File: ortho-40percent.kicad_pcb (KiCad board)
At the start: 2 copper layers, 229 x 81 mm, 128 parts, among them J1 USB-C_Receptacle-24, SW1 SW_NO_4-Pin, SW10 CherryMX, SW11 CherryMX, SW12 CherryMX, SW13 CherryMX, SW14 CherryMX, SW15 CherryMX, SW16 CherryMX, SW17 CherryMX, SW18 CherryMX, SW19 CherryMX, SW2 CherryMX, SW20 CherryMX, SW21 CherryMX, SW22 CherryMX, SW23 CherryMX, SW24 CherryMX, SW25 CherryMX, SW26 CherryMX, SW27 CherryMX, SW28 CherryMX, SW29 CherryMX, SW3 CherryMX, SW30 CherryMX, SW31 CherryMX, SW32 CherryMX, SW33 CherryMX, SW34 CherryMX, SW35 CherryMX, SW36 CherryMX, SW37 CherryMX, SW38 CherryMX, SW39 CherryMX, SW4 CherryMX, SW40 CherryMX, SW41 CherryMX, SW42 CherryMX, SW43 CherryMX, SW44 CherryMX, SW45 CherryMX, SW46 CherryMX, SW47 CherryMX, SW48 CherryMX, SW49 CherryMX, SW5 CherryMX, SW50 CherryMX, SW51 CherryMX, SW6 CherryMX, SW7 CherryMX, SW8 CherryMX, SW9 CherryMX, U1 U_TPD4E05U06DQAR, U2 U_ATmega32u4-MU, Y1 XTAL_4Lead

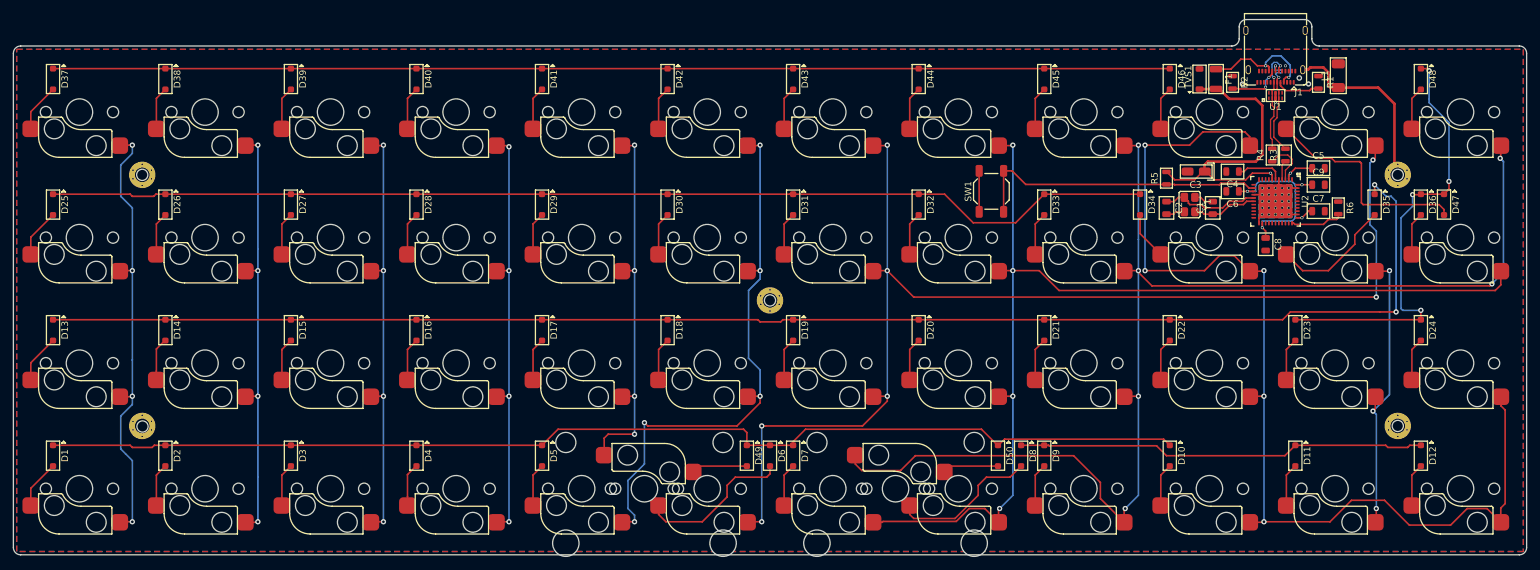
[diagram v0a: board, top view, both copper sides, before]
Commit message: Routing Finished
All connections routed. Focusing on cleaning up for length optimization and minimal bottom plane cutting.
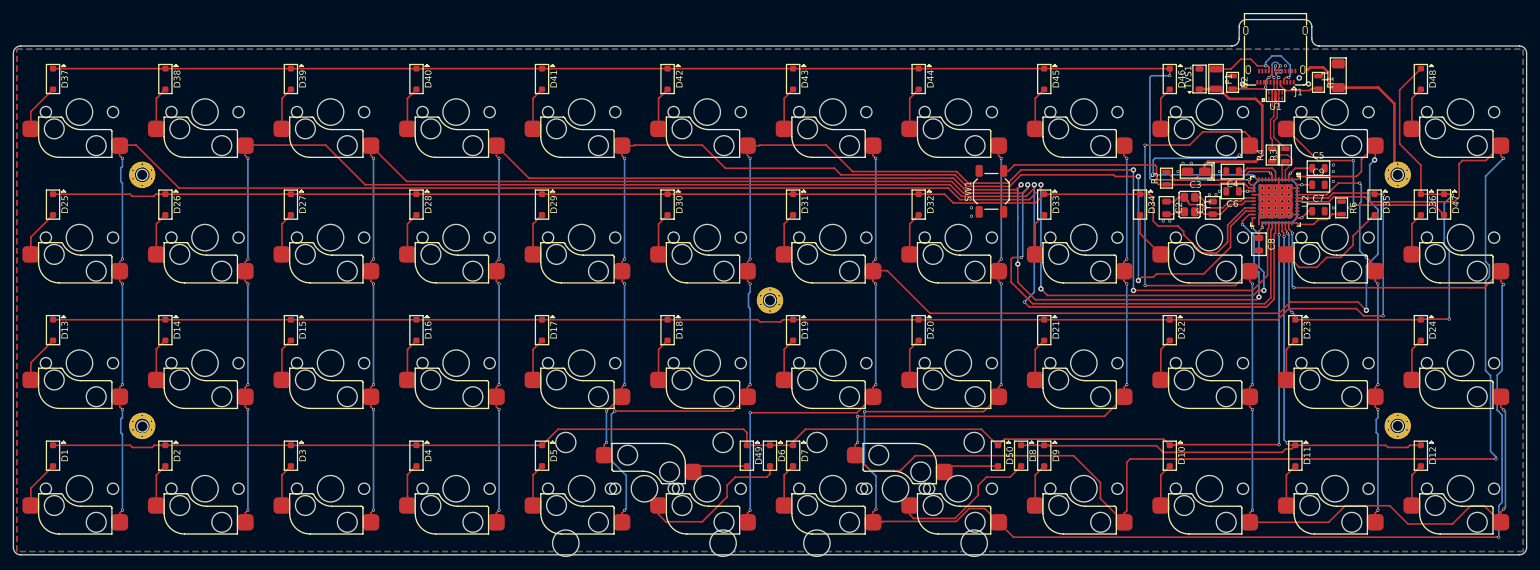
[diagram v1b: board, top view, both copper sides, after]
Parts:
- moved C8 1.00 mm to (228.5, 192.9)
- moved R6 0.50 mm to (241.0, 187.4)
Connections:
- D1 pad K: /KeyMatrix/ROW3 -> /ROW3
- D10 pad K: /KeyMatrix/ROW3 -> /ROW3
- D11 pad K: /KeyMatrix/ROW4 -> /ROW4
- D12 pad K: /KeyMatrix/ROW4 -> /ROW4
- D13 pad K: /KeyMatrix/ROW2 -> /ROW2
- D14 pad K: /KeyMatrix/ROW2 -> /ROW2
- D15 pad K: /KeyMatrix/ROW2 -> /ROW2
- D16 pad K: /KeyMatrix/ROW2 -> /ROW2
- D17 pad K: /KeyMatrix/ROW2 -> /ROW2
- D18 pad K: /KeyMatrix/ROW2 -> /ROW2
- D19 pad K: /KeyMatrix/ROW2 -> /ROW2
- D2 pad K: /KeyMatrix/ROW3 -> /ROW3
- D20 pad K: /KeyMatrix/ROW2 -> /ROW2
- D21 pad K: /KeyMatrix/ROW2 -> /ROW2
- D22 pad K: /KeyMatrix/ROW2 -> /ROW2
- D23 pad K: /KeyMatrix/ROW5 -> /ROW5
- D24 pad K: /KeyMatrix/ROW5 -> /ROW5
- D25 pad K: /KeyMatrix/ROW1 -> /ROW1
- D26 pad K: /KeyMatrix/ROW1 -> /ROW1
- D27 pad K: /KeyMatrix/ROW1 -> /ROW1
- D28 pad K: /KeyMatrix/ROW1 -> /ROW1
- D29 pad K: /KeyMatrix/ROW1 -> /ROW1
- D3 pad K: /KeyMatrix/ROW3 -> /ROW3
- D30 pad K: /KeyMatrix/ROW1 -> /ROW1
- D31 pad K: /KeyMatrix/ROW1 -> /ROW1
- D32 pad K: /KeyMatrix/ROW1 -> /ROW1
- D33 pad K: /KeyMatrix/ROW1 -> /ROW1
- D34 pad K: /KeyMatrix/ROW1 -> /ROW1
- D35 pad K: /KeyMatrix/ROW2 -> /ROW2
- D36 pad K: /KeyMatrix/ROW5 -> /ROW5
- D37 pad K: /KeyMatrix/ROW0 -> /ROW0
- D38 pad K: /KeyMatrix/ROW0 -> /ROW0
- D39 pad K: /KeyMatrix/ROW0 -> /ROW0
- D4 pad K: /KeyMatrix/ROW3 -> /ROW3
- D40 pad K: /KeyMatrix/ROW0 -> /ROW0
- D41 pad K: /KeyMatrix/ROW0 -> /ROW0
- D42 pad K: /KeyMatrix/ROW0 -> /ROW0
- D43 pad K: /KeyMatrix/ROW0 -> /ROW0
- D44 pad K: /KeyMatrix/ROW0 -> /ROW0
- D45 pad K: /KeyMatrix/ROW0 -> /ROW0
- D46 pad K: /KeyMatrix/ROW0 -> /ROW0
- D47 pad K: /KeyMatrix/ROW5 -> /ROW5
- D48 pad K: /KeyMatrix/ROW5 -> /ROW5
- D49 pad K: /KeyMatrix/ROW3 -> /ROW3
- D5 pad K: /KeyMatrix/ROW3 -> /ROW3
- D50 pad K: /KeyMatrix/ROW3 -> /ROW3
- D6 pad K: /KeyMatrix/ROW3 -> /ROW3
- D7 pad K: /KeyMatrix/ROW3 -> /ROW3
- D8 pad K: /KeyMatrix/ROW4 -> /ROW4
- D9 pad K: /KeyMatrix/ROW4 -> /ROW4
- SW1 pad 1: GND -> Net-(SW1-Pad1)
- SW1 pad 3: Net-(R5-Pad1) -> Net-(SW1-Pad3)
- SW10 pad 1: /KeyMatrix/COL8 -> /COL8
- SW11 pad 1: /KeyMatrix/COL9 -> /COL9
- SW12 pad 1: /KeyMatrix/COL10 -> /COL10
- SW13 pad 1: /KeyMatrix/COL9 -> /COL9
- SW14 pad 1: /KeyMatrix/COL0 -> /COL0
- SW15 pad 1: /KeyMatrix/COL1 -> /COL1
- SW16 pad 1: /KeyMatrix/COL2 -> /COL2
- SW17 pad 1: /KeyMatrix/COL3 -> /COL3
- SW18 pad 1: /KeyMatrix/COL4 -> /COL4
- SW19 pad 1: /KeyMatrix/COL5 -> /COL5
- SW2 pad 1: /KeyMatrix/COL0 -> /COL0
- SW20 pad 1: /KeyMatrix/COL6 -> /COL6
- SW21 pad 1: /KeyMatrix/COL7 -> /COL7
- SW22 pad 1: /KeyMatrix/COL8 -> /COL8
- SW23 pad 1: /KeyMatrix/COL9 -> /COL9
- SW24 pad 1: /KeyMatrix/COL10 -> /COL10
- SW25 pad 1: /KeyMatrix/COL9 -> /COL9
- SW26 pad 1: /KeyMatrix/COL0 -> /COL0
- SW27 pad 1: /KeyMatrix/COL1 -> /COL1
- SW28 pad 1: /KeyMatrix/COL2 -> /COL2
- SW29 pad 1: /KeyMatrix/COL3 -> /COL3
- SW3 pad 1: /KeyMatrix/COL1 -> /COL1
- SW30 pad 1: /KeyMatrix/COL4 -> /COL4
- SW31 pad 1: /KeyMatrix/COL5 -> /COL5
- SW32 pad 1: /KeyMatrix/COL6 -> /COL6
- SW33 pad 1: /KeyMatrix/COL7 -> /COL7
- SW34 pad 1: /KeyMatrix/COL8 -> /COL8
- SW35 pad 1: /KeyMatrix/COL9 -> /COL9
- SW36 pad 1: /KeyMatrix/COL10 -> /COL10
- SW37 pad 1: /KeyMatrix/COL7 -> /COL7
- SW38 pad 1: /KeyMatrix/COL0 -> /COL0
- SW39 pad 1: /KeyMatrix/COL1 -> /COL1
- SW4 pad 1: /KeyMatrix/COL2 -> /COL2
- SW40 pad 1: /KeyMatrix/COL2 -> /COL2
- SW41 pad 1: /KeyMatrix/COL3 -> /COL3
- SW42 pad 1: /KeyMatrix/COL4 -> /COL4
- SW43 pad 1: /KeyMatrix/COL5 -> /COL5
- SW44 pad 1: /KeyMatrix/COL6 -> /COL6
- SW45 pad 1: /KeyMatrix/COL7 -> /COL7
- SW46 pad 1: /KeyMatrix/COL8 -> /COL8
- SW47 pad 1: /KeyMatrix/COL9 -> /COL9
- SW48 pad 1: /KeyMatrix/COL6 -> /COL6
- SW49 pad 1: /KeyMatrix/COL8 -> /COL8
- SW5 pad 1: /KeyMatrix/COL3 -> /COL3
- SW50 pad 1: /KeyMatrix/COL4 -> /COL4
- SW51 pad 1: /KeyMatrix/COL8 -> /COL8
- SW6 pad 1: /KeyMatrix/COL5 -> /COL5
- SW7 pad 1: /KeyMatrix/COL6 -> /COL6
- SW8 pad 1: /KeyMatrix/COL7 -> /COL7
- SW9 pad 1: /KeyMatrix/COL7 -> /COL7
- U2 pad 1: Net-(U2-Pad1) -> /COL6
- U2 pad 11: Net-(U2-Pad11) -> /COL9
- U2 pad 12: Net-(U2-Pad12) -> /ROW0
- U2 pad 19: Net-(U2-Pad19) -> /ROW1
- U2 pad 20: Net-(U2-Pad20) -> /COL4
- U2 pad 21: Net-(U2-Pad21) -> /COL3
- U2 pad 22: Net-(U2-Pad22) -> /COL0
- U2 pad 26: Net-(U2-Pad26) -> /COL5
- U2 pad 27: Net-(U2-Pad27) -> /COL2
- U2 pad 28: Net-(U2-Pad28) -> /COL1
- U2 pad 29: Net-(U2-Pad29) -> /ROW3
- U2 pad 30: Net-(U2-Pad30) -> /ROW4
- U2 pad 31: Net-(U2-Pad31) -> /ROW5
- U2 pad 32: Net-(U2-Pad32) -> /COL7
- U2 pad 39: Net-(U2-Pad39) -> /COL8
- U2 pad 40: Net-(U2-Pad40) -> /ROW2
- U2 pad 41: Net-(U2-Pad41) -> /COL10
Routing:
- net /COL8: track 0.00 -> 287.6 mm, vias 0 -> 8
- net /COL0: track 0.00 -> 264.6 mm, vias 0 -> 10
- net /COL7: track 0.00 -> 258.7 mm, vias 0 -> 10
- net /COL1: track 0.00 -> 250.3 mm, vias 0 -> 8
- net /ROW2: track 0.00 -> 234.4 mm, vias 0 -> 2
- net /COL2: track 0.00 -> 230.2 mm, vias 0 -> 8
- net /KeyMatrix/ROW2: track 226.5 -> 0.00 mm, vias 2 -> 0
- net /ROW3: track 0.00 -> 225.6 mm, vias 0 -> 2
- net /COL3: track 0.00 -> 207.9 mm, vias 0 -> 10
- net /ROW0: track 0.00 -> 204.8 mm, vias 0 -> 2
- net /COL6: track 0.00 -> 195.9 mm, vias 0 -> 8
- net /ROW1: track 0.00 -> 193.8 mm
- net /COL9: track 0.00 -> 190.8 mm, vias 0 -> 10
- net /KeyMatrix/COL8: track 190.1 -> 0.00 mm, vias 6 -> 0
- net /COL5: track 0.00 -> 187.3 mm, vias 0 -> 8
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
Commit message: Electrical Finished
All electrical completed, refdes placed. Beginning to place silkscreen logos and other branding items.
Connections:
- U2 pad 20: /COL4 -> /COL5
- U2 pad 21: /COL3 -> /COL4
- U2 pad 22: /COL0 -> /COL3
- U2 pad 26: /COL5 -> /COL2
- U2 pad 27: /COL2 -> /COL1
- U2 pad 28: /COL1 -> /COL0
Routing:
- net /COL6: track 195.9 -> 242.6 mm
- net /COL5: track 187.3 -> 177.7 mm
- net /COL2: track 230.2 -> 224.3 mm
- net /COL1: track 250.3 -> 245.1 mm
- net /COL9: track 190.8 -> 187.1 mm
- net /ROW0: track 204.8 -> 202.5 mm
- net /COL4: track 169.7 -> 167.6 mm
- net /COL3: track 207.9 -> 205.8 mm, vias 10 -> 8
- net /COL7: track 258.7 -> 260.6 mm
- net /COL8: track 287.6 -> 286.0 mm
- net Net-(D6-PadA): track 23.9 -> 22.5 mm
- net /COL0: track 264.6 -> 265.8 mm, vias 10 -> 8
- net GNDPWR: track 28.4 -> 27.5 mm
- net /ROW3: track 225.6 -> 226.2 mm
- net /ROW5: track 84.7 -> 85.2 mm
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
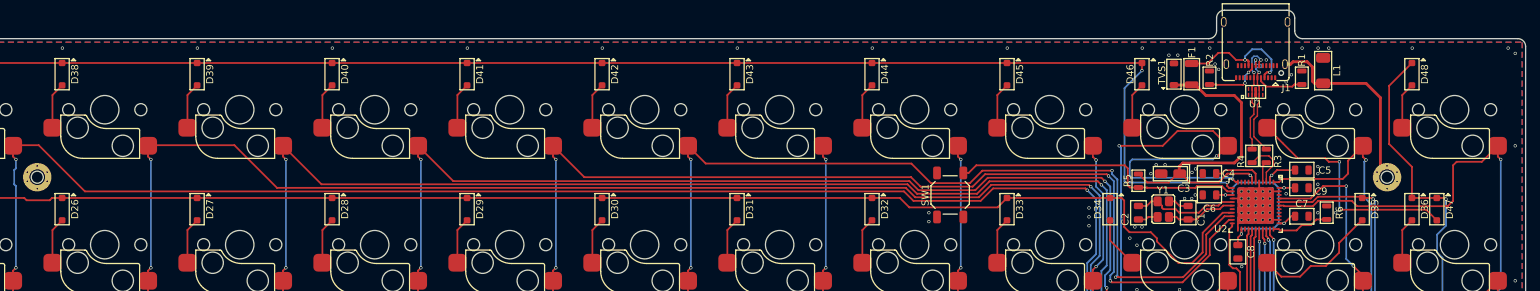
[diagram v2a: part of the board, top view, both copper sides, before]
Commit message: Hardware Complete
Electrical completed and DRC passed.
Silkscreen logos and info added.
Ready for first prototype ordering.
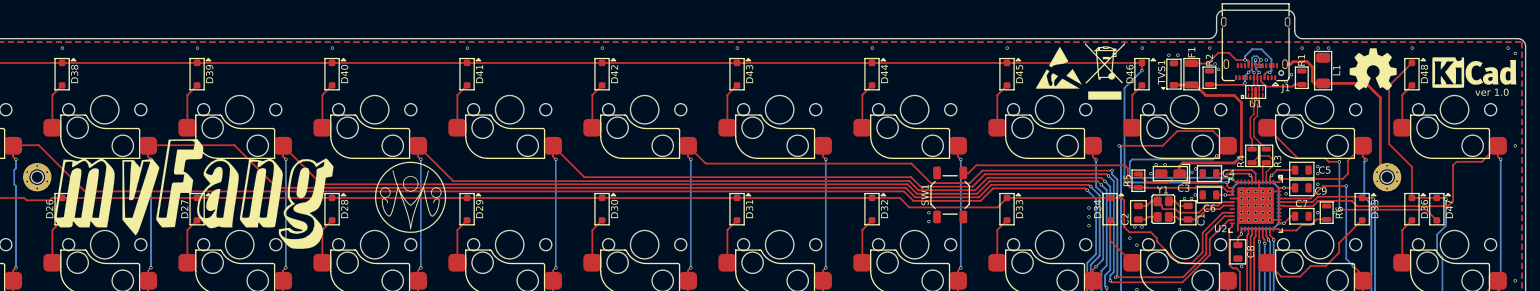
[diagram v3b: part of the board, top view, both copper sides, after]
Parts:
- added G***: LOGO, ortho-40percent:mvFang_logo, F.Cu at (81.5, 184.8)
- added G***: LOGO, jizzbot:jizzbot3000, F.Cu at (112.0, 185.2)
- added REF**: KiCAD Logo, Symbols:Symbol_KiCAD-Logo_CopperAndSilkScreenTop, F.Cu at (261.8, 167.5)
- added REF***: ESD-Logo_6.6x6mm_SilkScreen, Symbols:ESD-Logo_6.6x6mm_SilkScreen, F.Cu at (203.2, 167.0)
- added REF***: OSHW-Symbol_6.7x6mm_SilkScreen, Symbols:OSHW-Symbol_6.7x6mm_SilkScreen, F.Cu at (247.5, 167.2)
- added REF***: WEEE-Logo_5.6x8mm_SilkScreen, Symbols:WEEE-Logo_5.6x8mm_SilkScreen, F.Cu at (209.8, 167.5)
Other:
- board text added: "ver 1.0"

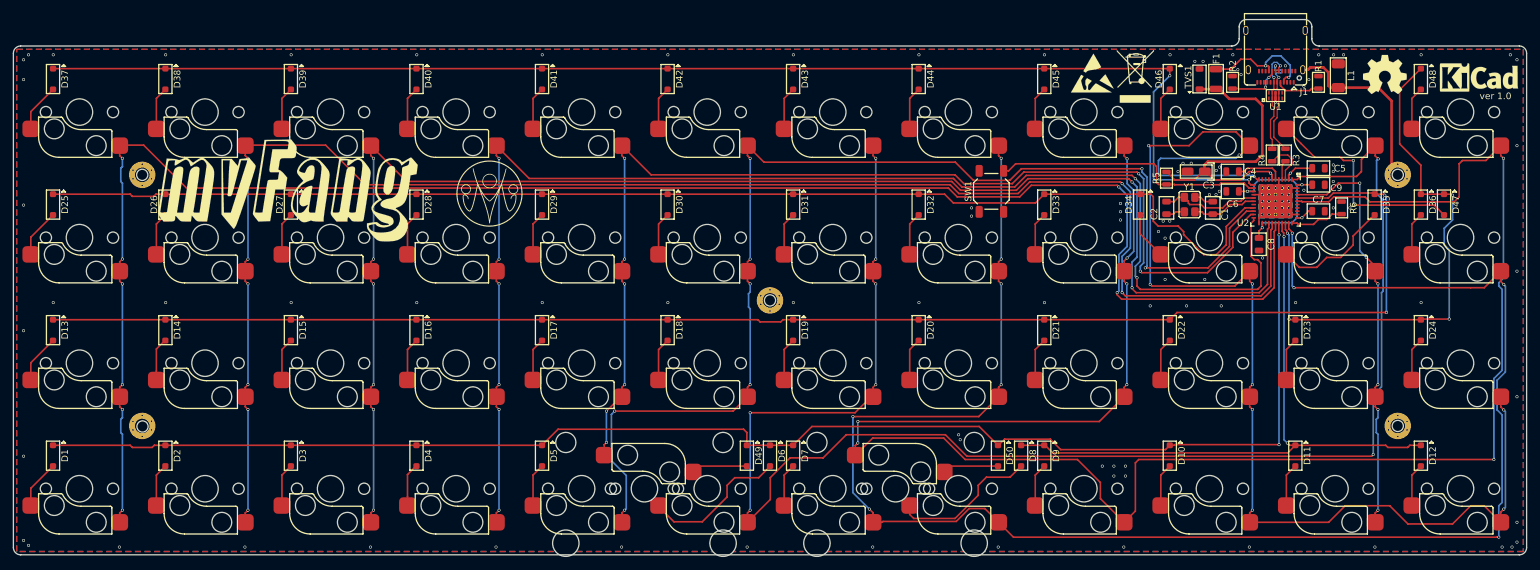
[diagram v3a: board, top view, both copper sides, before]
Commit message: Mounting hole modifications
Drilled holes for mounting holes were smaller than 0.3mm which many boardhouses charge extra for. Increased hole size to 0.33mm.
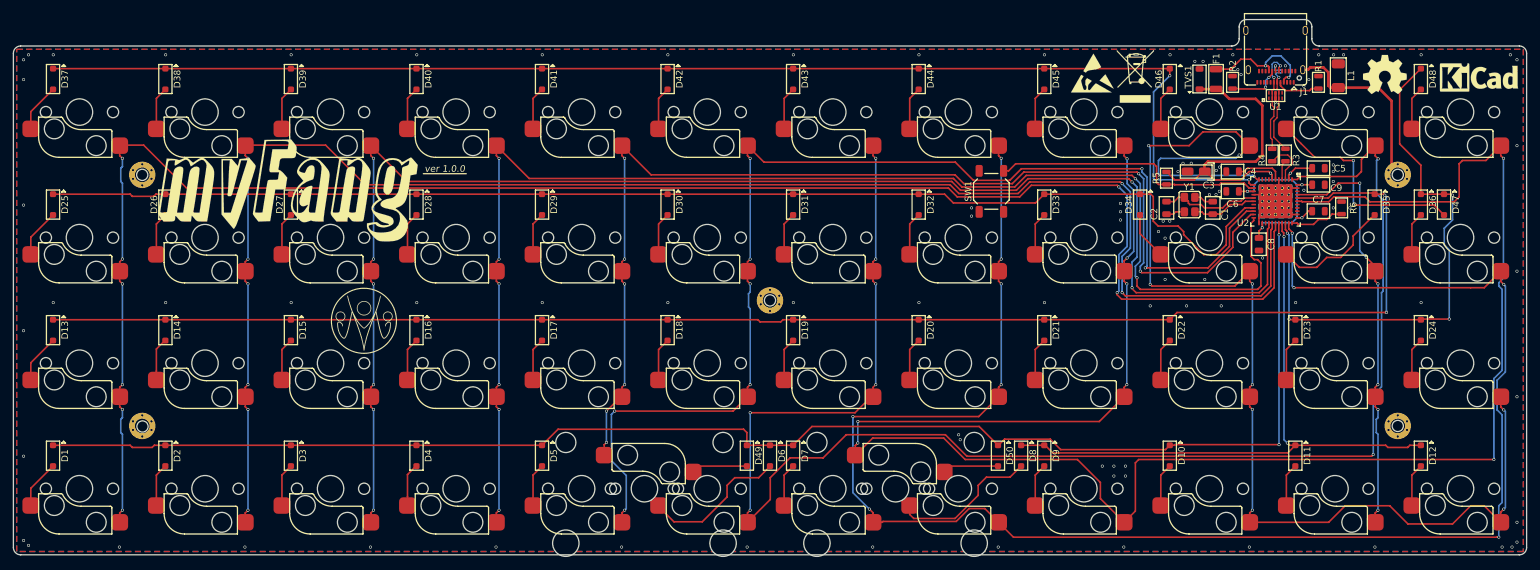
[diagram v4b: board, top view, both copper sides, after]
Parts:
- moved G*** 27.0 mm to (93.0, 204.5)
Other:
- board text added: "ver 1.0.0"
- board text removed: "ver 1.0"
